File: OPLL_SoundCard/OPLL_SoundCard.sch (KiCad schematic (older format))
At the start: 31 parts, among them J1 AudioJack3, P1 Digital, P10 CONN_01X01, P11 CONN_01X01, P12 CONN_01X01, P13 CONN_01X01, P2 Power, P3 Analog, P4 Analog, P5 PWM, P6 PWM, P7 Communication, P8 CONN_01X01, P9 CONN_01X01, U1 YM2413B, U2 LMC660, Y1 3.57MHz

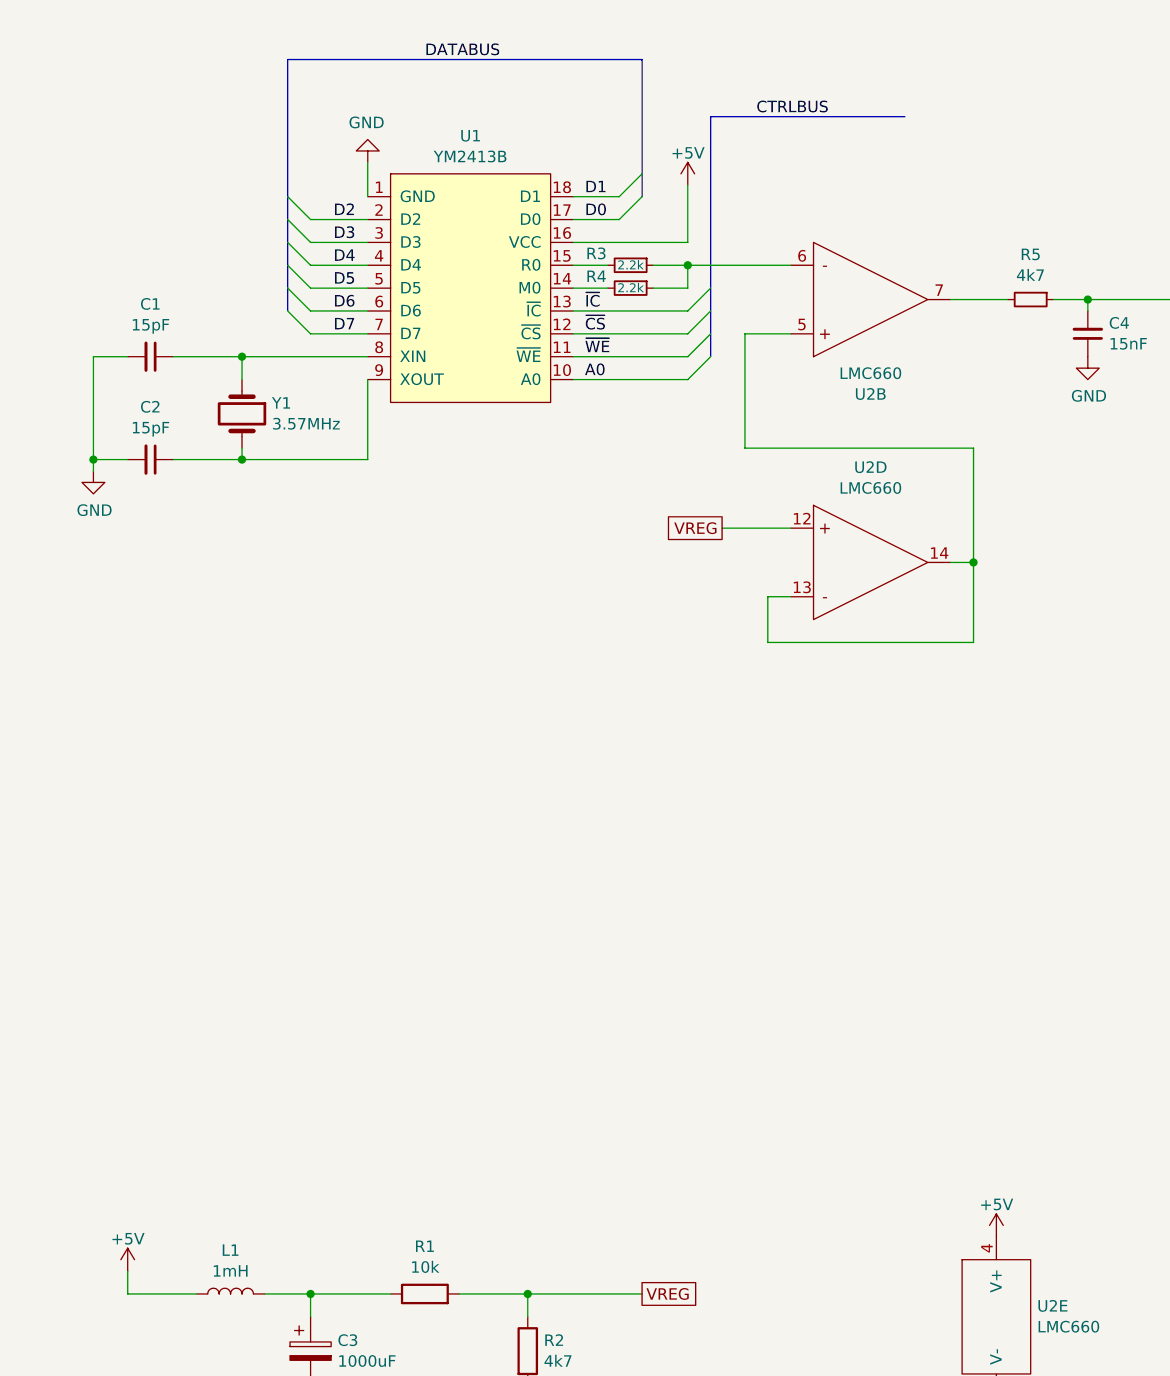
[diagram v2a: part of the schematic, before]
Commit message: PCB Soundcard
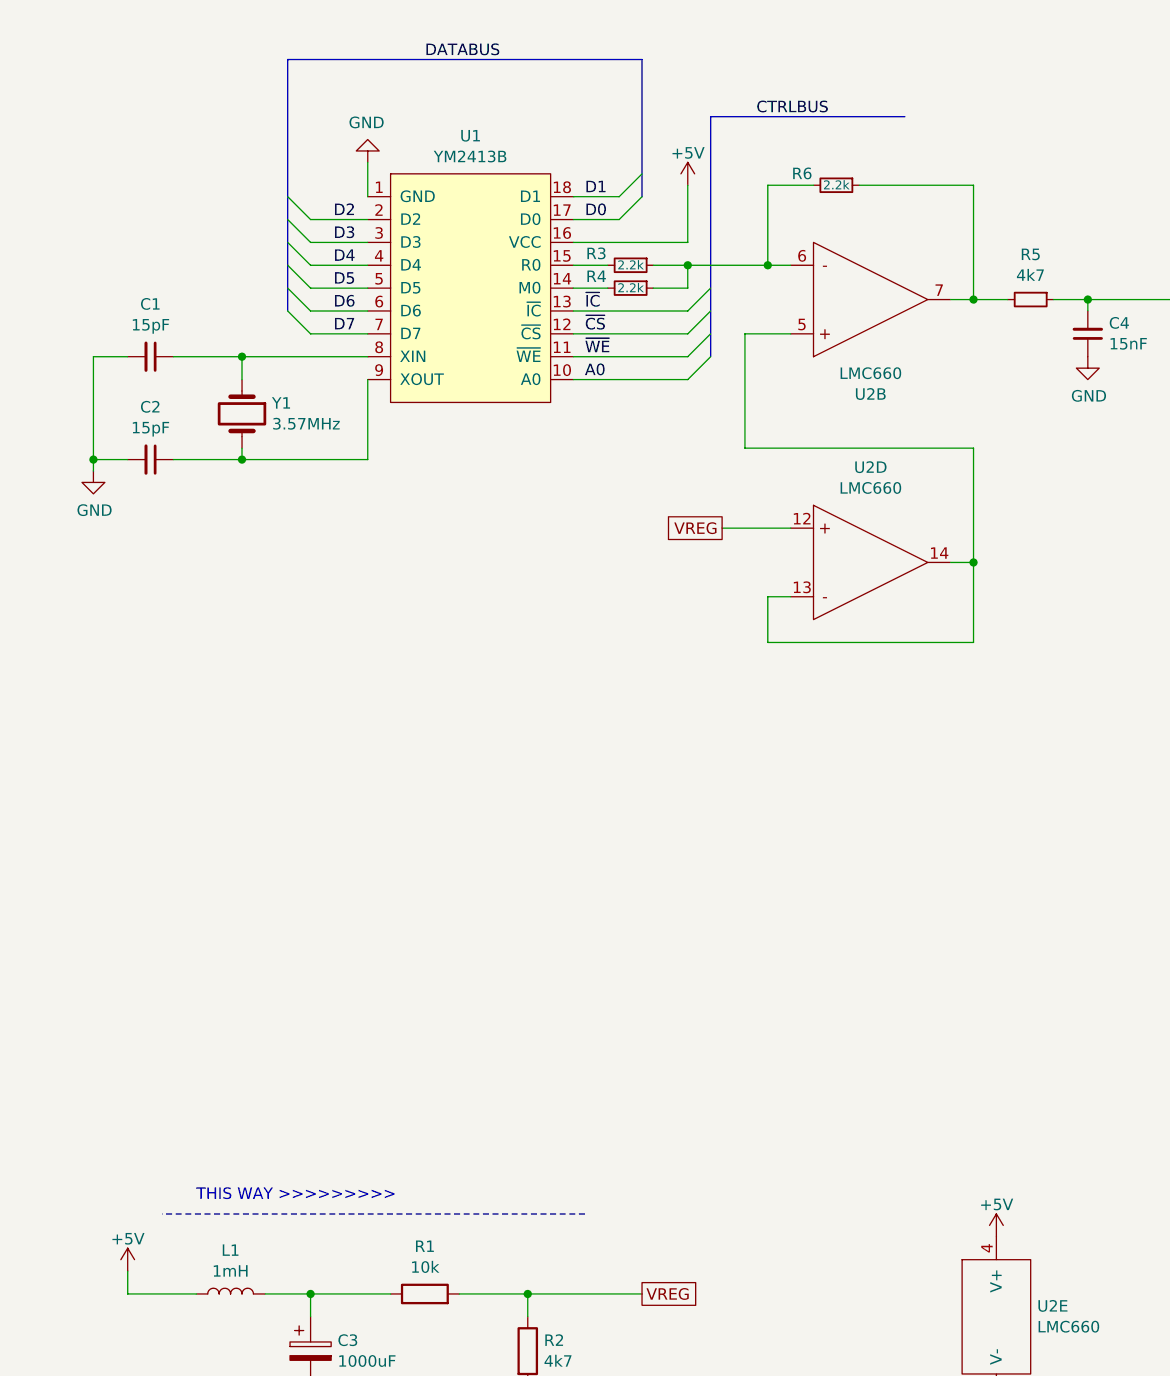
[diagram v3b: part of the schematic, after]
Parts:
- added R6: 2.2k, Resistor_SMD:R_0805_2012Metric_Pad1.20x1.40mm_HandSolder, symbol Device:R_Small
- J1: footprint Connector_Audio:Jack_3.5mm_PJ320D_Horizontal -> Connector_Audio:Jack_3.5mm_CUI_SJ-3523-SMT_Horizontal
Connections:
- net at R3.1, R4.1, U2.6: now also R6.2
- net at R5.2, U2.7: now also R6.1
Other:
- note added: "THIS WAY >>>>>>>>>"
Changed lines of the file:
@@
 	5450 2750 5450 3350
 Wire Wire Line
-	4350 2750 4600 2750
-Wire Wire Line
-	3200 2600 3650 2600
+	4350 2750 4450 2750
+Wire Wire Line
+	3200 2600 3550 2600
 Wire Wire Line
 	3650 2900 3450 2900
@@
 F 0 "J1" H 7220 2783 50  0000 R CNN
 F 1 "AudioJack3" H 7220 2874 50  0000 R CNN
-F 2 "Connector_Audio:Jack_3.5mm_PJ320D_Horizontal" H 7500 2850 50  0001 C CNN
+F 2 "Connector_Audio:Jack_3.5mm_CUI_SJ-3523-SMT_Horizontal" H 7500 2850 50  0001 C CNN
 F 3 "~" H 7500 2850 50  0001 C CNN
 	1    7500 2850
@@
 	1    0    0    -1
 $EndComp
+$Comp
+L Device:R_Small R6
+U 1 1 5FE0C91C
+P 3850 2250
+F 0 "R6" V 3800 2100 50  0000 C CNN
+F 1 "2.2k" V 3850 2250 39  0000 C CNN
+F 2 "Resistor_SMD:R_0805_2012Metric_Pad1.20x1.40mm_HandSolder" H 3850 2250 50  0001 C CNN
+F 3 "~" H 3850 2250 50  0001 C CNN
+	1    3850 2250
+	0    1    1    0
+$EndComp
+Wire Wire Line
+	3550 2600 3550 2250
+Wire Wire Line
+	3550 2250 3750 2250
+Connection ~ 3550 2600
+Wire Wire Line
+	3550 2600 3650 2600
+Wire Wire Line
+	3950 2250 4450 2250
+Wire Wire Line
+	4450 2250 4450 2750
+Connection ~ 4450 2750
+Wire Wire Line
+	4450 2750 4600 2750
+Wire Notes Line
+	2750 6750 900  6750
 Wire Bus Line
 	3000 1700 3000 2300
@@
 Wire Bus Line
 	8800 3500 8800 4600
+Text Notes 1050 6700 0    50   ~ 0
+THIS WAY >>>>>>>>>
 $EndSCHEMATC
